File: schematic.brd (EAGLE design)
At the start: 160 x 100 mm, 87 parts, among them J1 MEGAFIT-4SKT-RA, J10 JST-PA-SMT-RA-4, J11 JST-PA-SMT-RA-2, J12 JST-PA-SMT-RA-2, J14 JST-PA-SMT-RA-2, J15 JST-PA-SMT-RA-2, J17 JST-PA-SMT-RA-3, J18 JST-PA-SMT-RA-3, J19 JST-PA-SMT-RA-4, J20 JST-PA-SMT-RA-4, J21 JST-PA-SMT-RA-3, J22 JST-PA-SMT-RA-3, J3 DF13-6, J4 DF13-5, J5 DF13-6, J6 SSW-116-02-S-TRA, J7 SSW-108-02-S-TRA, J8 SSW-108-02-S-D-RA, J9 SSW-106-02-S-D-RA, SW1 M2022LL2W13, SW2 M2022LL2W13, U1 VHE100W, U11 MED_MOSFET, U2 VHB150W, U4 INA139, U5 INA139, U6 INA139, U7 RELAY, U8 RELAY, U9 RELAY

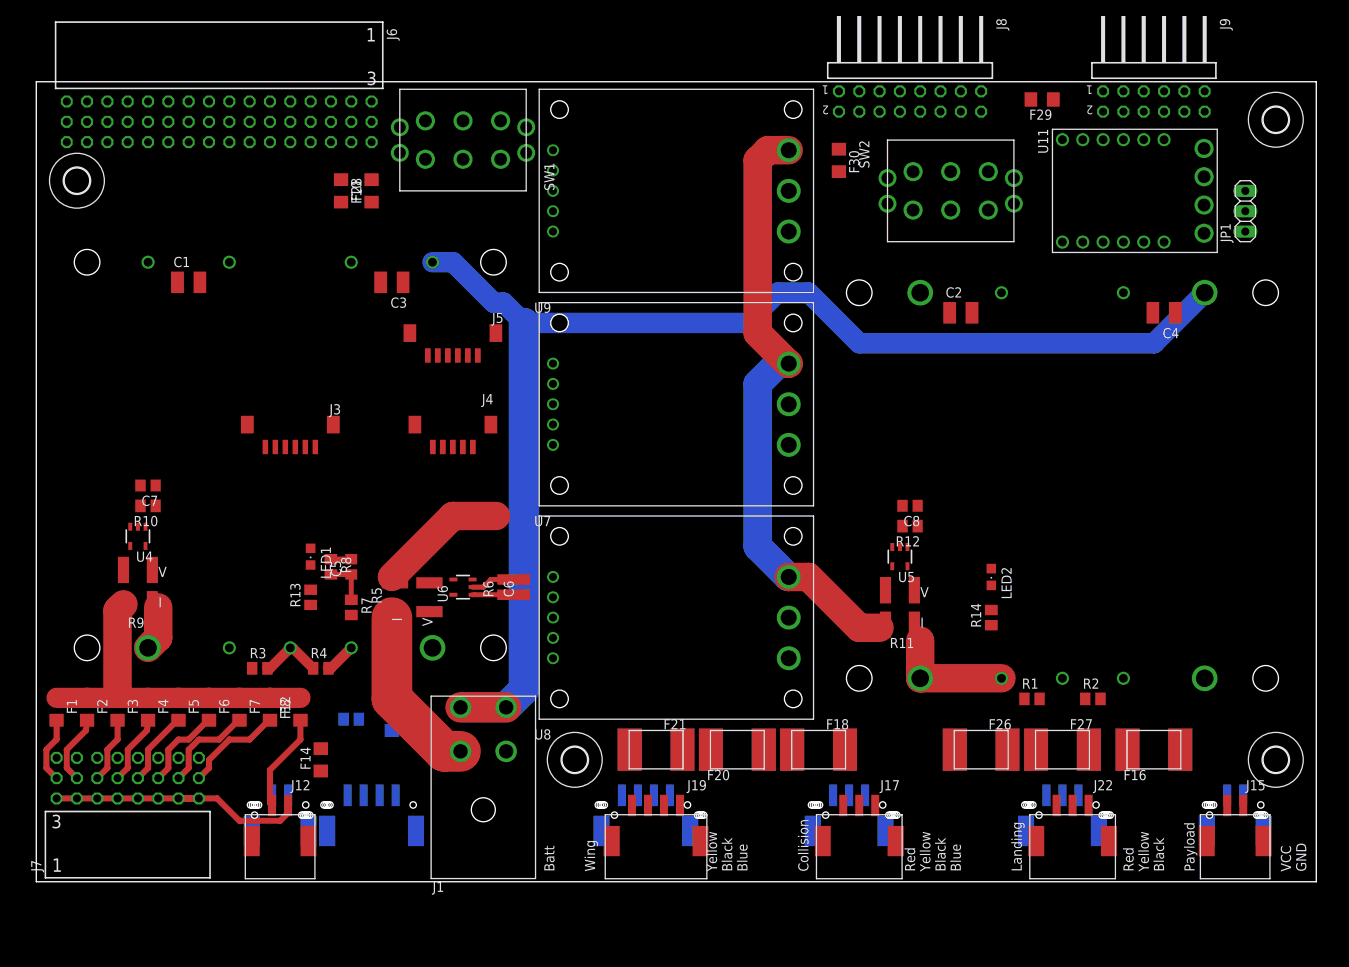
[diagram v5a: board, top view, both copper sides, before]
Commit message: Silkscreen adjustments, cleanup prior to autoroute.
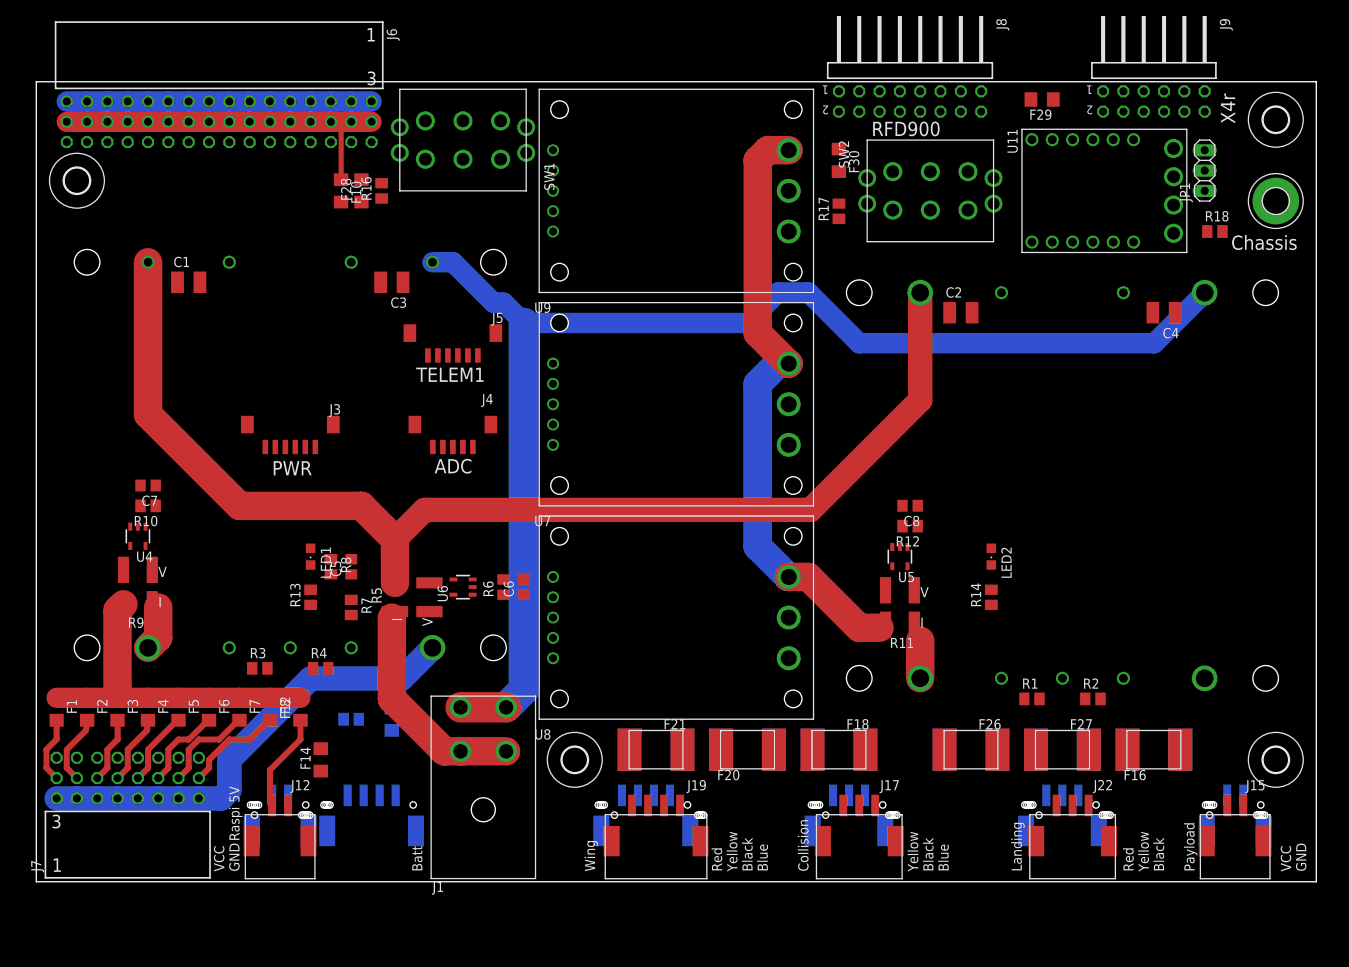
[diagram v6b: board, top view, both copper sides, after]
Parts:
- added H1: MOUNT-PAD-ROUND3.2, holes:3,2-PAD
- added R16, R17, R18: (no value), rcl:M0805
- moved JP1 7.18 mm to (146.1, 88.9)
- moved U11 3.81 mm to (130.8, 86.4)
- moved LED2 2.54 mm to (119.4, 40.6)
- moved R14 2.54 mm to (119.4, 35.6)
- moved F18 2.54 mm to (100.3, 16.5)
- moved F19 2.54 mm to (100.3, 16.5)
- moved SW2 2.54 mm to (111.8, 86.4)
- moved F20 1.27 mm to (88.9, 16.5)
- moved F23 1.27 mm to (88.9, 16.5)
- moved F25 1.27 mm to (116.8, 16.5)
- moved F26 1.27 mm to (116.8, 16.5)
- moved F28 1.27 mm to (40.6, 86.4)
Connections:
- new net N$37: H1.B3,2, R18.2
- new net N$38: R17.2, SW2.GND1, SW2.GND2, SW2.GND3, SW2.GND4
- new net N$39: R16.2, SW1.GND1, SW1.GND2, SW1.GND3, SW1.GND4
- net GND: now also R16.1, R17.1, R18.1; no longer SW1.GND1, SW1.GND2, SW1.GND3, SW1.GND4, SW2.GND1, SW2.GND2, SW2.GND3, SW2.GND4
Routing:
- net V+: track 16.2 -> 148.1 mm
- net GND: track 47.3 -> 96.3 mm
- net N$5: track 0.00 -> 45.3 mm
- net N$21: track 14.9 -> 4.70 mm
- net N$8: track 7.85 -> 0.00 mm
- net CUR_MEAS: track 6.42 -> 0.00 mm
- net V_MEAS: track 5.72 -> 0.00 mm
- net N$25: track 21.5 -> 27.2 mm
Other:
- board text added: "ADC"
- board text added: "Chassis"
- board text added: "Lidar-Lite"
- board text added: "PWR"
- board text added: "RFD900"
- board text added: "Raspi 5V"
- board text added: "TELEM1"
- board text added: "VID 5V"
- board text added: "X4r"

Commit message: Autorouted and ground plane poured.
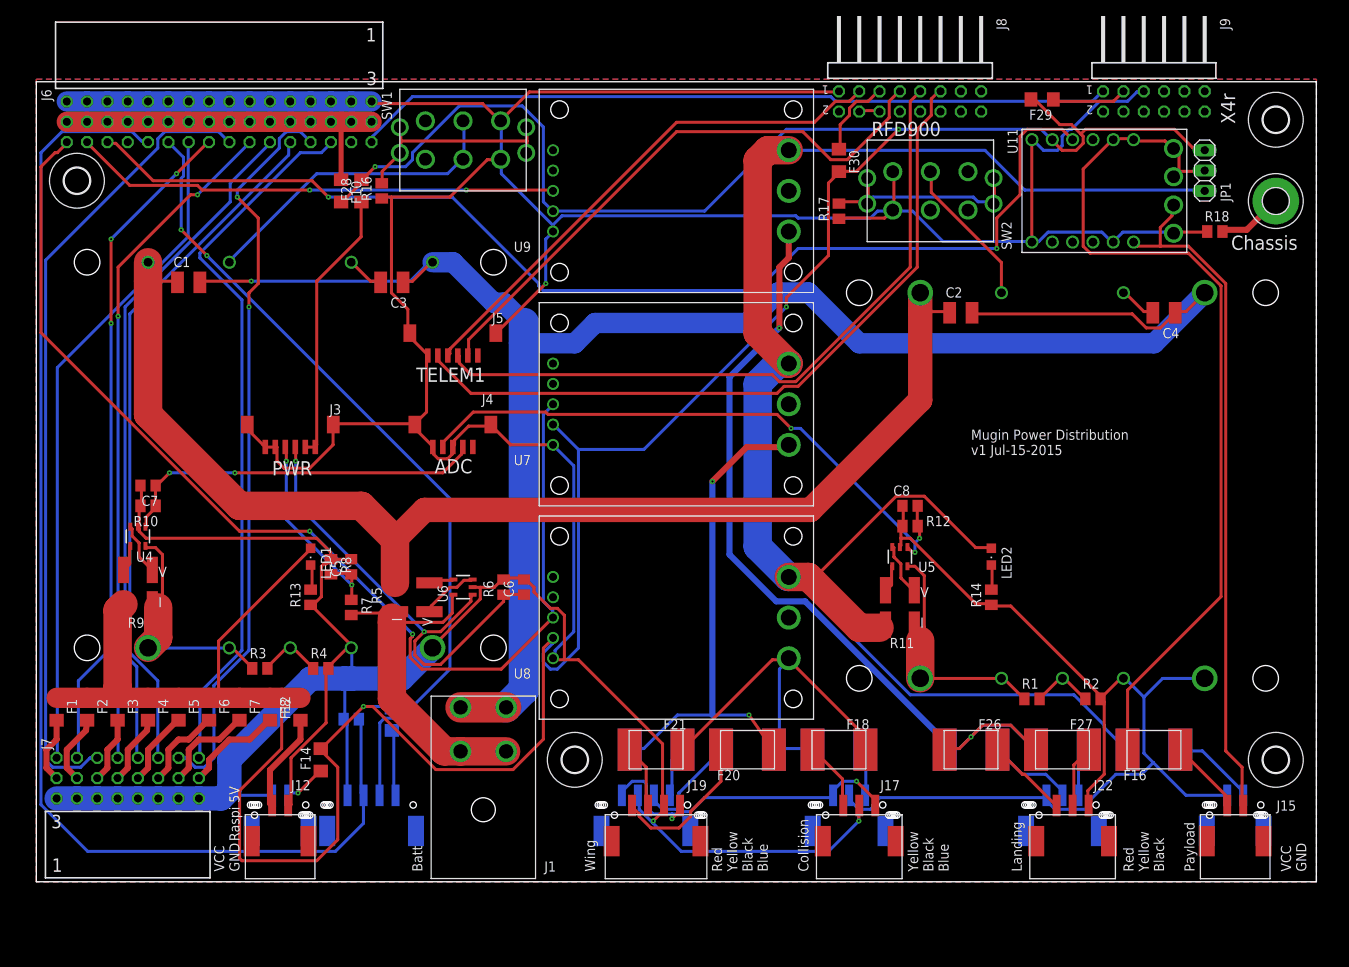
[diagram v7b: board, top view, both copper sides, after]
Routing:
- net GND: track 96.3 -> 773.6 mm, vias 0 -> 3
- net +5V: track 41.3 -> 408.7 mm, vias 0 -> 4
- net AUX5: track 0.00 -> 154.0 mm
- net AUX3: track 0.00 -> 143.9 mm, vias 0 -> 2
- net AUX1: track 0.00 -> 139.2 mm, vias 0 -> 2
- net +24V: track 76.2 -> 212.3 mm
- net N$4: track 0.00 -> 113.5 mm
- net VCC_TAXI: track 0.00 -> 109.1 mm, vias 0 -> 2
- net AUX6: track 0.00 -> 101.3 mm, vias 0 -> 2
- net MAIN3: track 0.00 -> 100.6 mm
- net RC_SIG: track 0.00 -> 94.9 mm
- net MAIN7: track 0.00 -> 93.2 mm, vias 0 -> 2
- net RRTS: track 0.00 -> 92.1 mm
- net MAIN8: track 0.00 -> 89.7 mm
- net RTX: track 0.00 -> 86.8 mm
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- added copper zone on layer 1, net GND
- added copper zone on layer 16, net GND
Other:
- board text added: "Mugin Power Distribution v1 Jul-15-2015"

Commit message: DRC checks completed.
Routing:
- net VCC_TAXI: track 109.1 -> 113.6 mm
